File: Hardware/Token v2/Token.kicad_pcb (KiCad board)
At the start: 2 copper layers, 20.1 x 11.2 mm, 8 parts, among them J2 Conn_01x04_Female, J4 Conn_02x04_Odd_Even, U1 ATtiny202-SS

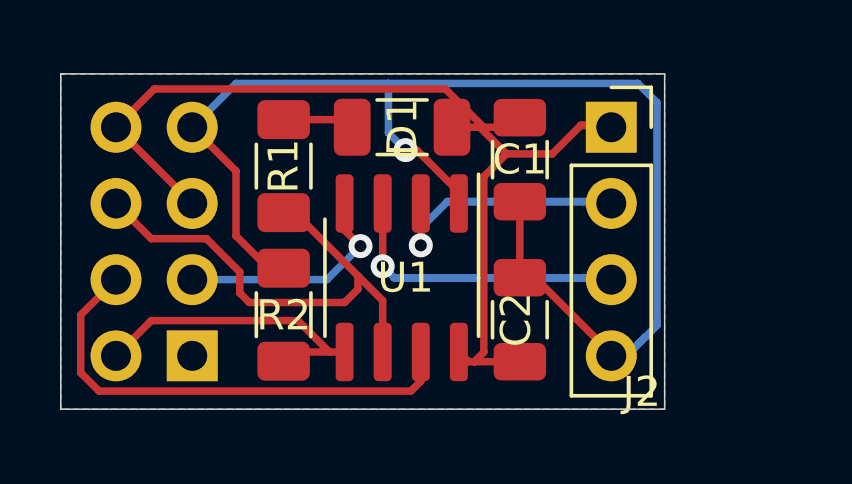
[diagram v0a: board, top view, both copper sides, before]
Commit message: Created a new version of the hardware token v2
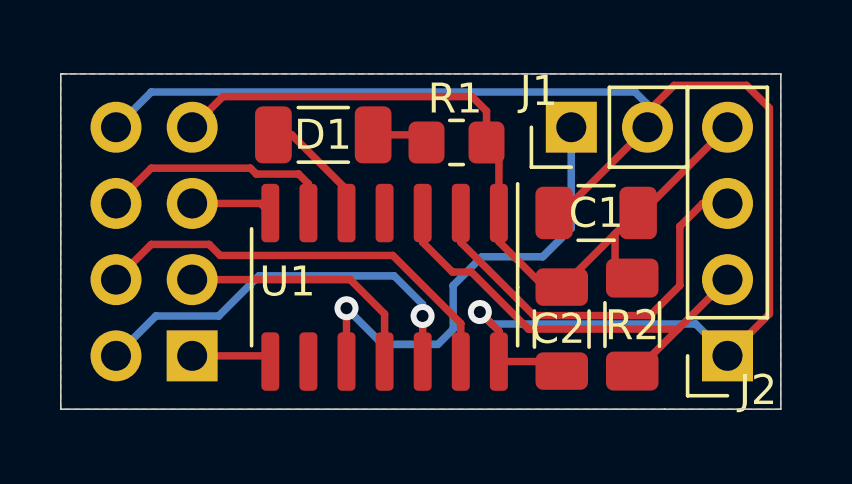
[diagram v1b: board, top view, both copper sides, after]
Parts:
- added J1: Conn_01x02_Male, Connector_PinHeader_2.54mm:PinHeader_1x02_P2.54mm_Vertical, F.Cu at (155.0, 38.3)
- R1: footprint Resistor_SMD:R_1206_3216Metric_Pad1.30x1.75mm_HandSolder -> Resistor_SMD:R_0805_2012Metric_Pad1.20x1.40mm_HandSolder
- R2: value 100k -> 500k
- U1: value ATtiny202-SS -> ATtiny1604-SS; footprint Package_SO:SOIC-8_3.9x4.9mm_P1.27mm -> Package_SO:SOIC-14_3.9x8.7mm_P1.27mm
- moved R2 11.6 mm to (157.0, 44.9)
- moved J2 8.55 mm to (160.2, 45.9), turned to 180 degrees
- moved R1 5.82 mm to (151.2, 38.8), turned to 0 degrees
- moved C1 3.10 mm to (155.8, 41.1), turned to 180 degrees
- moved D1 2.64 mm to (146.7, 38.5), turned to 0 degrees
- moved C2 1.43 mm to (154.7, 45.0)
- moved U1 0.65 mm to (148.8, 43.6)
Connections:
- C1 pad 2: CSN -> GND
- C2 pad 2: CSN -> GND
- D1 pad 1: CSN -> Net-(D1-Pad1)
- J2 pad 1: CSN -> GND
- J4 pad 8: CSN -> GND
- R1 pad 2: CE -> VCC
- R2 pad 1: MISO -> DATA_TOP
- U1 pad 2: DATA_TOP -> DATA_TOP_CLK
- U1 pad 3: DATA_TOP_CLK -> DATA_TOP
- U1 pad 4: DATA_BOTTOM -> Net-(U1-Pad4)
- U1 pad 5: MISO -> Net-(D1-Pad1)
- U1 pad 7: DATA_BOTTOM_CLK -> CSN
- U1 pad 8: CSN -> IRQ
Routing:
- net GND: track 0.00 -> 50.5 mm, vias 0 -> 1
- net CSN: track 35.0 -> 2.74 mm
- net VCC: track 45.2 -> 27.5 mm, vias 1 -> 0
- net UPDI: track 0.00 -> 15.6 mm, vias 0 -> 1
- net CE: track 16.7 -> 8.09 mm
- net Net-(D1-Pad1): track 0.00 -> 3.97 mm
- net DATA_TOP_CLK: track 17.1 -> 13.6 mm, vias 1 -> 0
- net MISO: track 10.2 -> 13.6 mm, vias 0 -> 1
- net IRQ: track 0.00 -> 2.68 mm
- net DATA_BOTTOM_CLK: track 16.3 -> 14.3 mm
- net DATA_TOP: track 14.2 -> 15.2 mm, vias 1 -> 0
- net DATA_BOTTOM: track 7.71 -> 8.47 mm, vias 1 -> 0
- net Net-(D1-Pad2): track 2.39 -> 1.88 mm
- added copper zone on B.Cu, net GND
- added copper zone on F.Cu, net GND
- removed copper zone on B.Cu, net CSN
- removed copper zone on F.Cu, net CSN
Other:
- board size 20.1 x 11.2 mm -> 24 x 11.2 mm
- board text added: "09042021"
- board text added: "B/CLK"
- board text added: "B/DATA"
- board text added: "ETI v2.1 Smart Energy"
- board text added: "GND"
- board text added: "T/CLK"
- board text added: "T/DATA"
- board text added: "VCC"
- board text removed: "24032021"
- board text removed: "ETI v2.0 Smart Energy"
